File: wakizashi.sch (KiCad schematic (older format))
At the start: 14 parts, among them SW1 SW_Push, U1 ATmega32U4-AU, Y1 16MHz

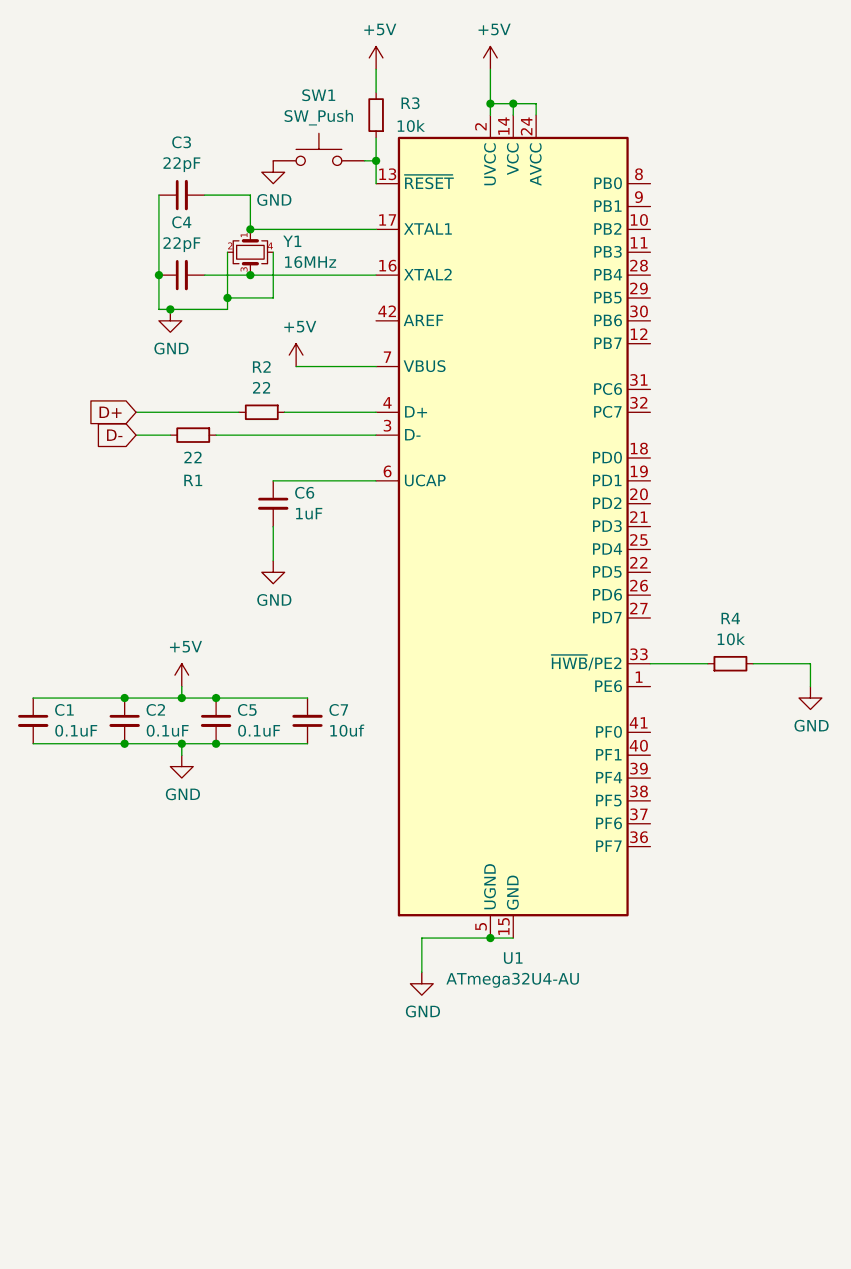
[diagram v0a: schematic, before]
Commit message: Swap Proton C in
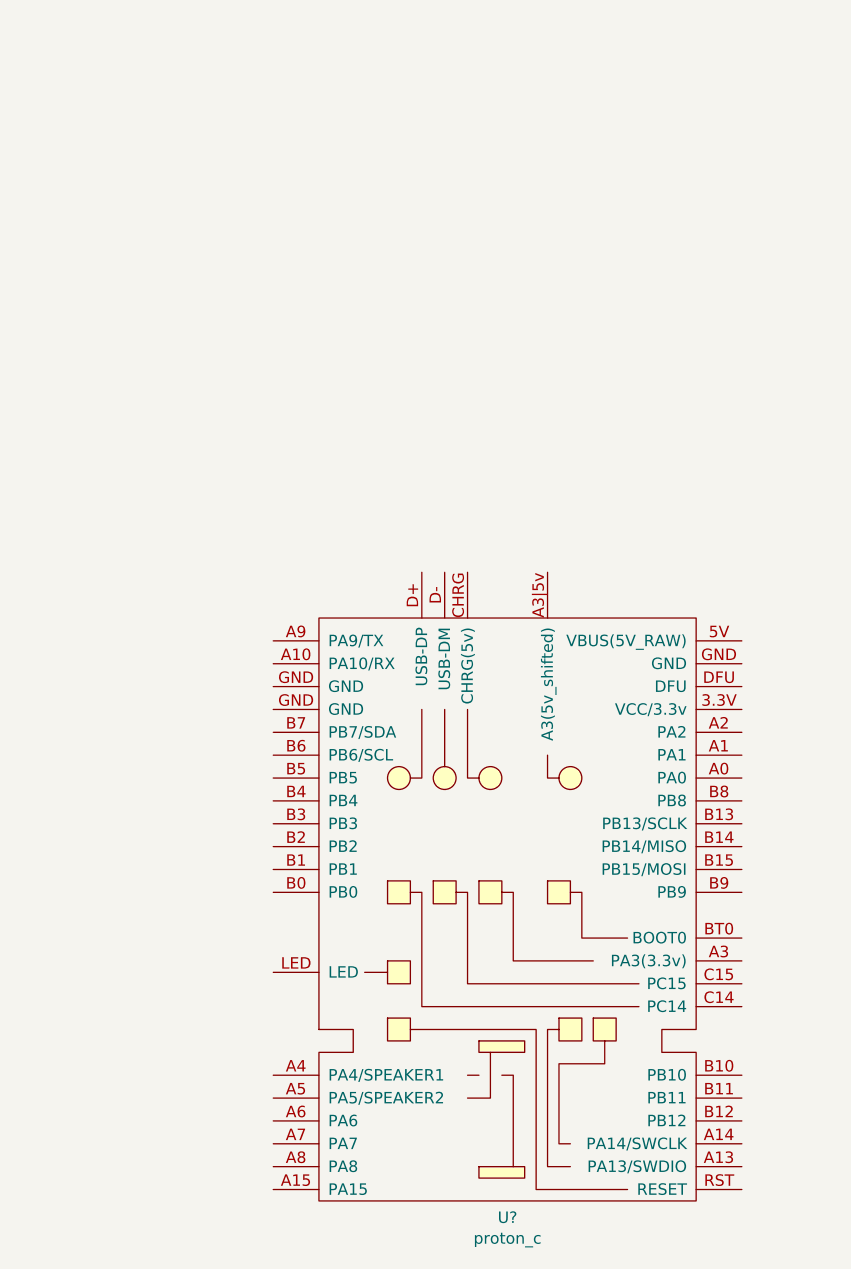
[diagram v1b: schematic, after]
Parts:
- removed C1, C2, C5: 0.1uF, Capacitor_THT:CP_Radial_D4.0mm_P1.50mm, symbol Device:C_Small
- removed C3, C4: 22pF, Capacitor_THT:CP_Radial_D4.0mm_P1.50mm, symbol Device:C_Small
- removed C6: 1uF, Capacitor_THT:CP_Radial_D4.0mm_P1.50mm, symbol Device:C_Small
- removed C7: 10uf, Capacitor_THT:CP_Radial_D4.0mm_P1.50mm, symbol Device:C_Small
- removed R1, R2: 22, symbol Device:R_Small
- removed R3, R4: 10k, symbol Device:R_Small
- removed SW1: SW_Push, Button_Switch_THT:SW_PUSH_6mm_H4.3mm, symbol Switch:SW_Push
- removed U1: ATmega32U4-AU, Package_QFP:TQFP-44_10x10mm_P0.8mm, symbol MCU_Microchip_ATmega:ATmega32U4-AU
- removed Y1: 16MHz, Crystal:Crystal_SMD_2520-4Pin_2.5x2.0mm, symbol Device:Crystal_GND24_Small
- added U?: proton_c, symbol proton_c:proton_c

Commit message: Add switch matrix
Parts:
- added D1, D10, D11, D12, D13, D14, D15, D16, D17, D18, D19, D2, D20, D21, D22, D23, D24, D25, D26, D27, D28, D29, D3, D30, D31, D32, D33, D34, D35, D36, D37, D38, D39, D4, D40, D41, D42, D43, D44, D45, D46, D47, D48, D5, D6, D7, D8, D9: D_Small, symbol Device:D_Small
- added MX1, MX10, MX11, MX12, MX13, MX14, MX15, MX16, MX17, MX18, MX19, MX2, MX20, MX21, MX22, MX23, MX24, MX25, MX26, MX27, MX28, MX29, MX3, MX30, MX31, MX32, MX33, MX34, MX35, MX36, MX37, MX38, MX39, MX4, MX40, MX41, MX42, MX43, MX44, MX45, MX46, MX47, MX48, MX5, MX6, MX7, MX8, MX9: MX-NoLED, symbol MX_Alps_Hybrid:MX-NoLED
- U1: renamed from U?; symbol proton_c:proton_c -> wakizashi-rescue:proton_c-proton_c
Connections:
- net labels added: COL0, COL1, COL10, COL11, COL2, COL3, COL4, COL5, COL6, COL7, COL8, COL9, ROW0, ROW1, ROW2, ROW3
- wire segments 0 -> 192

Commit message: Add switches and diodes
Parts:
- D1, D10, D11, D12, D13, D14, D15, D16, D17, D18, D19, D2, D20, D21, D22, D23, D24, D25, D26, D27, D28, D29, D3, D30, D31, D32, D33, D34, D35, D36, D37, D38, D39, D4, D40, D41, D42, D43, D44, D45, D46, D47, D48, D5, D6, D7, D8, D9: footprint (none) -> Diode_THT:D_A-405_P7.62mm_Horizontal
- MX1, MX10, MX11, MX12, MX13, MX14, MX15, MX16, MX17, MX18, MX19, MX2, MX20, MX21, MX22, MX23, MX24, MX25, MX26, MX27, MX28, MX29, MX3, MX30, MX31, MX32, MX33, MX34, MX35, MX36, MX37, MX38, MX39, MX4, MX40, MX41, MX42, MX43, MX44, MX45, MX46, MX47, MX48, MX5, MX6, MX7, MX8, MX9: footprint (none) -> MX_Alps_Hybrid-master:MX-1U
- U1: footprint (none) -> proton_c:proton_c
